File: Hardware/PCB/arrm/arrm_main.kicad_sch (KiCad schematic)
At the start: 47 parts

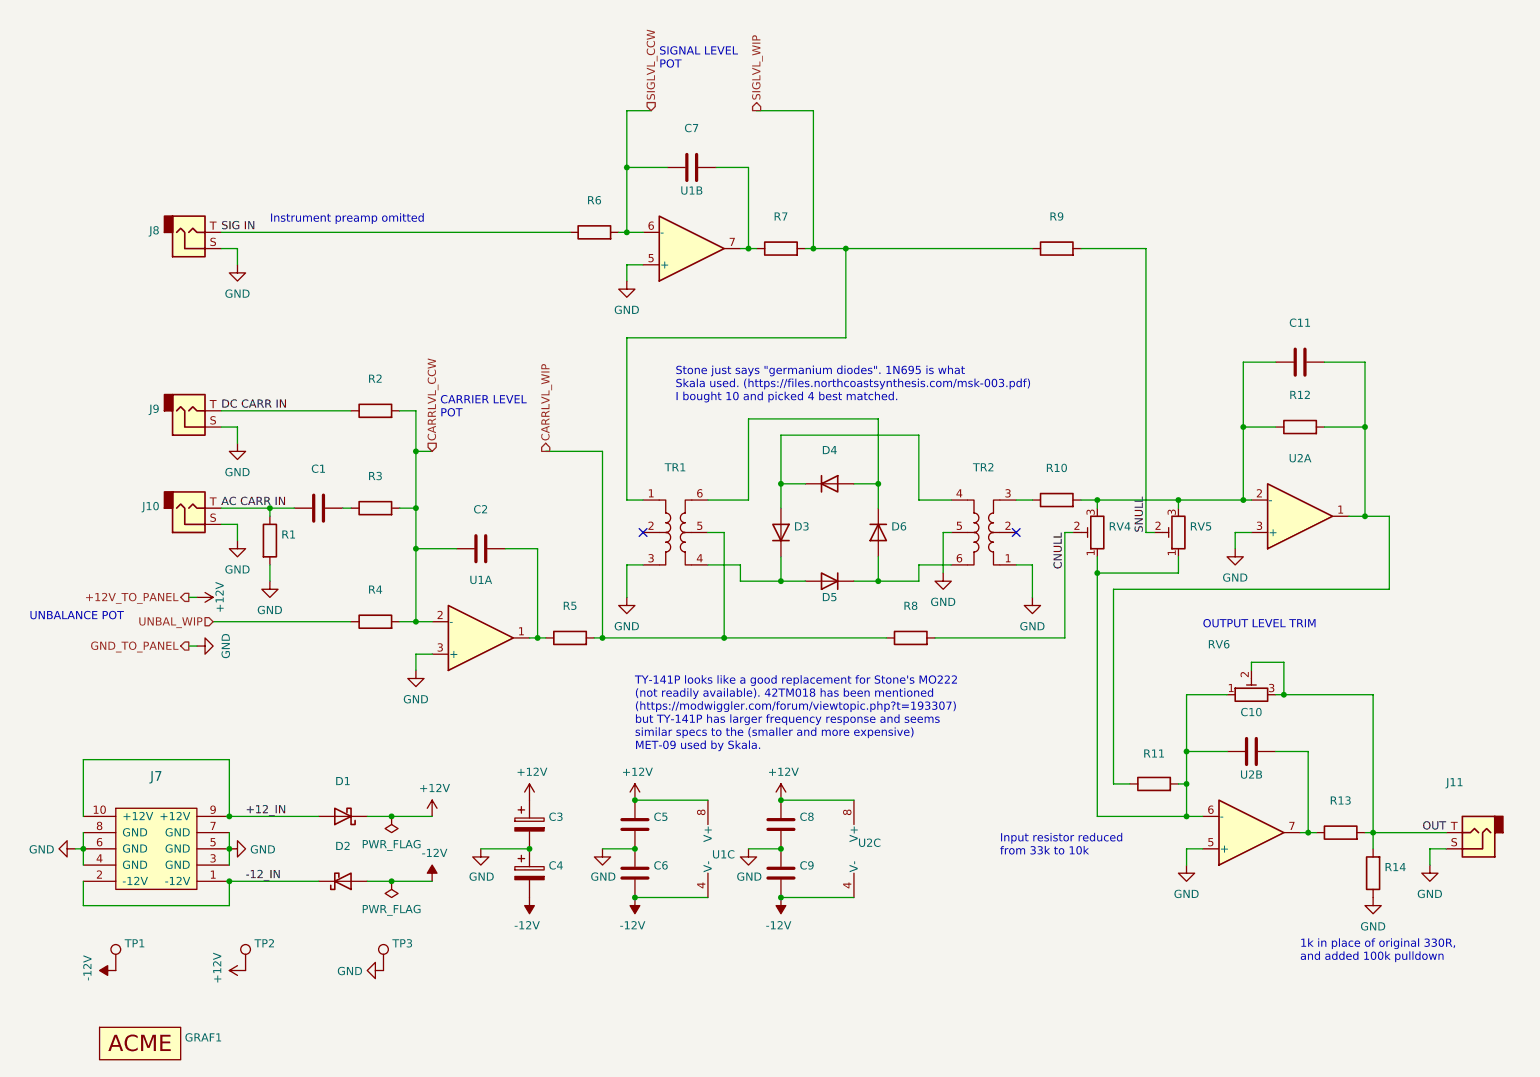
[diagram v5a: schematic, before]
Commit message: R4 should be 330k
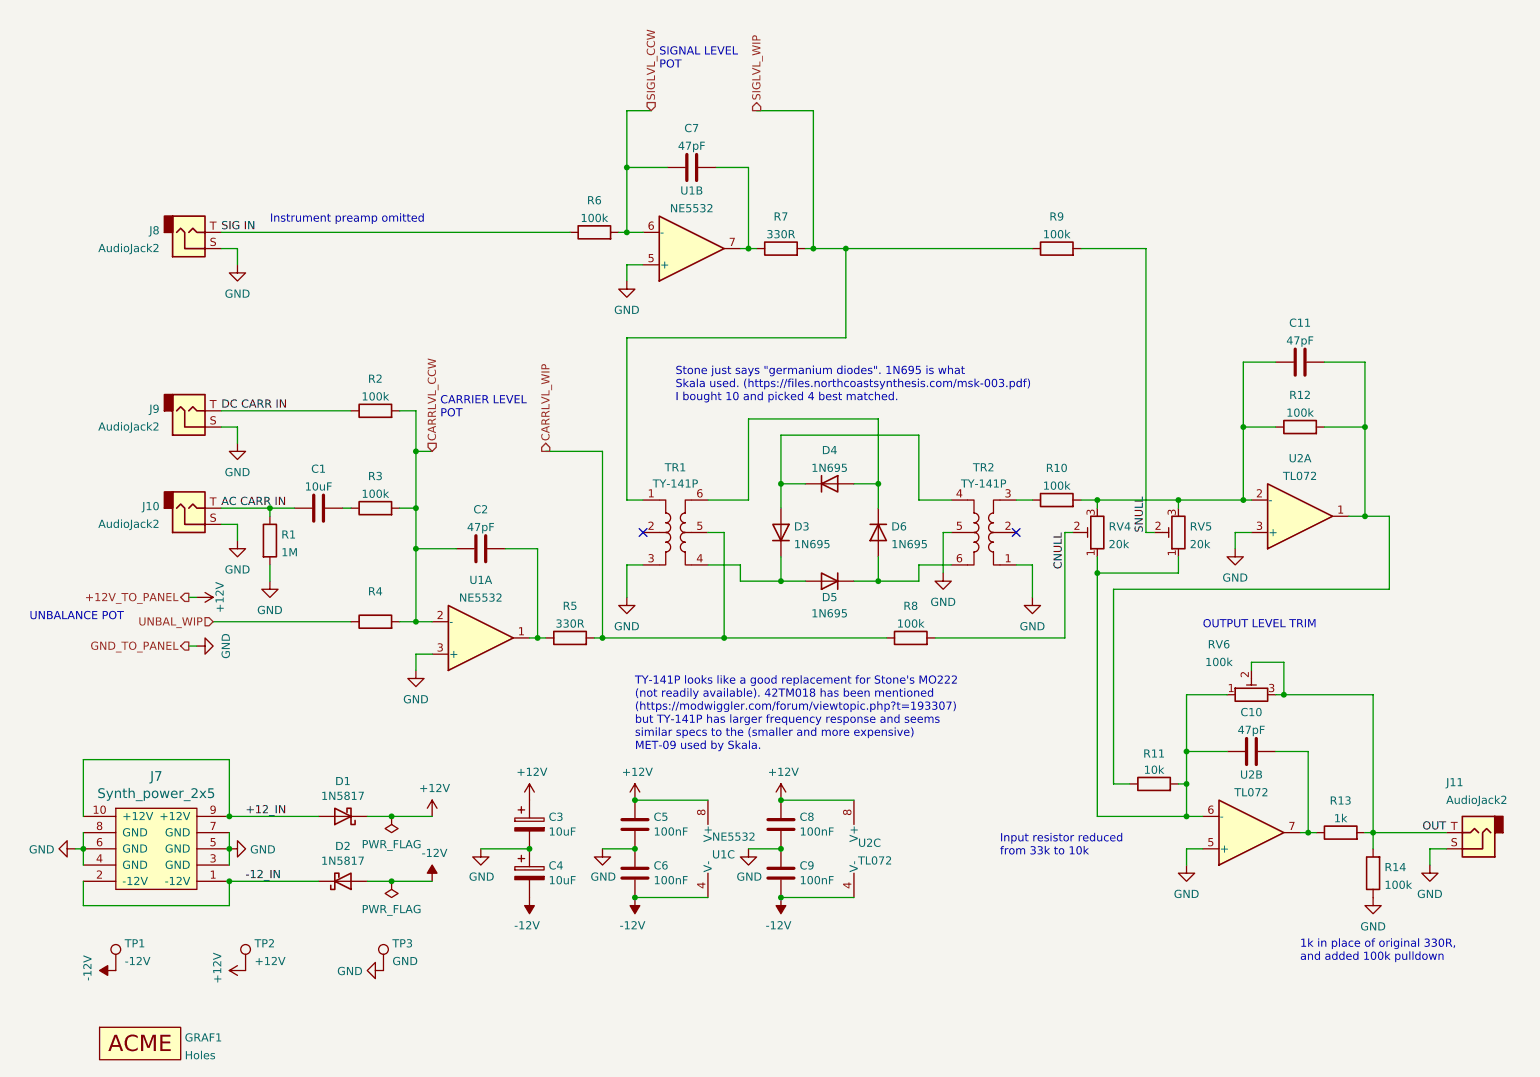
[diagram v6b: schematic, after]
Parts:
- C1: value (none) -> 10uF; footprint (none) -> ao_tht:C_Radial_D8.0mm_H11.5mm_P3.50mm
- C10, C11, C2, C7: value (none) -> 47pF; footprint (none) -> ao_tht:C_Disc_D5.0mm_W2.5mm_P5.00mm
- C3, C4: value (none) -> 10uF; footprint (none) -> ao_tht:CP_Radial_D6.3mm_P2.50mm
- C5, C6, C8, C9: value (none) -> 100nF; footprint (none) -> ao_tht:C_Disc_D3.0mm_W1.6mm_P2.50mm
- D1, D2: value (none) -> 1N5817; footprint (none) -> ao_tht:D_DO-41_SOD81_P10.16mm_Horizontal
- D3, D4, D5, D6: value (none) -> 1N695; footprint (none) -> ringmod:D_DO-7_P10.16mm_Horizontal
- GRAF1: value (none) -> Holes; footprint (none) -> ringmod:ringmod_panel_2_holes
- J10, J11, J8, J9: value (none) -> AudioJack2; footprint (none) -> ao_tht:Jack_6.35mm_PJ_629HAN_slots
- J7: value (none) -> Synth_power_2x5; footprint (none) -> ao_tht:Power_Header
- R1: value (none) -> 1M; footprint (none) -> ao_tht:R_Axial_DIN0207_L6.3mm_D2.5mm_P10.16mm_Horizontal
- R10, R12, R14, R2, R3, R6, R8, R9: value (none) -> 100k; footprint (none) -> ao_tht:R_Axial_DIN0207_L6.3mm_D2.5mm_P10.16mm_Horizontal
- R11: value (none) -> 10k; footprint (none) -> ao_tht:R_Axial_DIN0207_L6.3mm_D2.5mm_P10.16mm_Horizontal
- R13: value (none) -> 1k; footprint (none) -> ao_tht:R_Axial_DIN0207_L6.3mm_D2.5mm_P10.16mm_Horizontal
- R4: footprint (none) -> ao_tht:R_Axial_DIN0207_L6.3mm_D2.5mm_P10.16mm_Horizontal
- R5, R7: value (none) -> 330R; footprint (none) -> ao_tht:R_Axial_DIN0207_L6.3mm_D2.5mm_P10.16mm_Horizontal
- RV4, RV5: value (none) -> 20k; footprint (none) -> ao_tht:Potentiometer_Bourns_3296W_Vertical_standard
- RV6: value (none) -> 100k; footprint (none) -> ao_tht:Potentiometer_Bourns_3296W_Vertical_standard
- TP1: value (none) -> -12V; footprint (none) -> ao_tht:TestPoint_THTPad_D1.5mm_Drill0.7mm
- TP2: value (none) -> +12V; footprint (none) -> ao_tht:TestPoint_THTPad_D1.5mm_Drill0.7mm
- TP3: value (none) -> GND; footprint (none) -> ao_tht:TestPoint_THTPad_1.5x1.5mm_Drill0.7mm
- TR1, TR2: value (none) -> TY-141P; footprint (none) -> ringmod:Transformer_TY-141P
- U1: value (none) -> NE5532; footprint (none) -> ao_tht:DIP-8_W7.62mm_Socket_LongPads
- U2: value (none) -> TL072; footprint (none) -> ao_tht:DIP-8_W7.62mm_Socket_LongPads
